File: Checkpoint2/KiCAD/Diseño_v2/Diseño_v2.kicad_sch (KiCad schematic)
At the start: 0 parts

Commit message: PCB LDO (final?)
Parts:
- added Gen_In1, TP_GND1, TP_Out_PD1, TP_Vo1, TP_Vx1: (no value), Connector_PinHeader_2.54mm:PinHeader_1x01_P2.54mm_Vertical, symbol Connector:TestPoint
- added J1, J2: Conn_01x02, TerminalBlock:TerminalBlock_MaiXu_MX126-5.0-02P_1x02_P5.00mm, symbol Connector_Generic:Conn_01x02
- added J3: Conn_01x03, Connector_PinHeader_2.54mm:PinHeader_1x03_P2.54mm_Vertical, symbol Connector_Generic:Conn_01x03
- added J_FC1, J_LC1, J_LT1: (no value), TestPoint:TestPoint_2Pads_Pitch2.54mm_Drill0.8mm, symbol Jumper:Jumper_2_Bridged
- added Q1, Q2, Q5, Q7, Q8, Q9: BC547, Package_TO_SOT_THT:TO-92_Inline, symbol Transistor_BJT:BC547
- added Q3, Q4: BC557, Package_TO_SOT_THT:TO-92_Inline, symbol Transistor_BJT:BC557
- added Q6: TIP32A, Package_TO_SOT_THT:TO-220-3_Vertical, symbol Transistor_BJT:Q_PNP_BCE
- added R1, RE1, RE2, RE3, RE4: 680, Resistor_THT:R_Axial_DIN0207_L6.3mm_D2.5mm_P7.62mm_Horizontal, symbol Device:R
- added R2: 4k7, Resistor_THT:R_Axial_DIN0207_L6.3mm_D2.5mm_P7.62mm_Horizontal, symbol Device:R
- added R3, R4, Rx1: 10k, Resistor_THT:R_Axial_DIN0207_L6.3mm_D2.5mm_P7.62mm_Horizontal, symbol Device:R
- added RS1: 1.8, Resistor_THT:R_Axial_DIN0414_L11.9mm_D4.5mm_P15.24mm_Horizontal, symbol Device:R
- added RS2: 2.2, Resistor_THT:R_Axial_DIN0414_L11.9mm_D4.5mm_P15.24mm_Horizontal, symbol Device:R
- added Rf1: 10k, Resistor_THT:R_Axial_DIN0207_L6.3mm_D2.5mm_P2.54mm_Vertical, symbol Device:R
- added Ro1: 150, Resistor_THT:R_Axial_DIN0207_L6.3mm_D2.5mm_P7.62mm_Horizontal, symbol Device:R
- added Rref1: 1k2, Resistor_THT:R_Axial_DIN0207_L6.3mm_D2.5mm_P7.62mm_Horizontal, symbol Device:R
- added Rx2: 3k9, Resistor_THT:R_Axial_DIN0207_L6.3mm_D2.5mm_P7.62mm_Horizontal, symbol Device:R
- added TP_Vref1: (no value), symbol Connector:TestPoint
- added U1: TL431LP, Package_TO_SOT_THT:TO-92_Inline, symbol Reference_Voltage:TL431LP
- added U2: LM358, Package_DIP:DIP-8_W7.62mm_LongPads, symbol Amplifier_Operational:LM358
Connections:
- new net: Rf1.1, Ro1.2, Rref1.2, U2.2 (-)
- new net: Rx1.2, Rx2.2, U2.3 (+)
- new net: J1.2 (Pin_2), Q6.3 (E), R1.1, R2.1, RE1.1, RE2.1, U2.8 (V+)
- new net: J_LT1.1 (A), Q2.2 (B)
- new net: J_LT1.2 (B), R3.1, R4.1
- new net: Q2.1 (C), Q4.1 (C), Q5.2 (B), Q9.1 (C), TP_Out_PD1.1
- new net: J_LC1.1 (A), Q9.2 (B)
- new net: Q1.1 (C), Q3.1 (C), Q3.2 (B), Q4.2 (B)
- new net: Q3.3 (E), RE1.2
- new net: Q7.3 (E), RE4.1
- new net: Q8.3 (E), RE3.1
- new net: Gen_In1.1, J3.1 (Pin_1)
- new net: J_FC1.2 (B), Q7.1 (C)
- new net: Q7.2 (B), Q8.1 (C), Q8.2 (B), R2.2
- new net: J_FC1.1 (A), Q1.3 (E), Q2.3 (E)
- new net: Q5.1 (C), Q6.1 (B)
- new net: Q4.3 (E), RE2.2
- new net: J3.3 (Pin_3), R1.2, U1.1 (REF), U1.3 (K)
- new net GND: J1.1 (Pin_1), J2.1 (Pin_1), Q9.3 (E), R4.2, RE3.2, RE4.2, Rx2.1, TP_GND1.1, U1.2 (A), U2.4 (V-)
- new net Vf: J_LC1.2 (B), Rf1.2, U2.1
- new net Vo: J2.2 (Pin_2), R3.2, RS1.2, RS2.2, Ro1.1, TP_Vo1.1
- new net Vref: J3.2 (Pin_2), Q1.2 (B), Rref1.1, TP_Vref1.1
- new net Vx: Q5.3 (E), Q6.2 (C), RS1.1, RS2.1, Rx1.1, TP_Vx1.1
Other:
- note added: "Nota sobre las aberviaciones: LC: Lazo de corriente LT: Lazo de tensión PD: par diferencial FC: fuente de corriente"
- company: (none) -> FIUBA - TA138
- title: (none) -> Fuente regulada con protección Foldback - Grupo 5

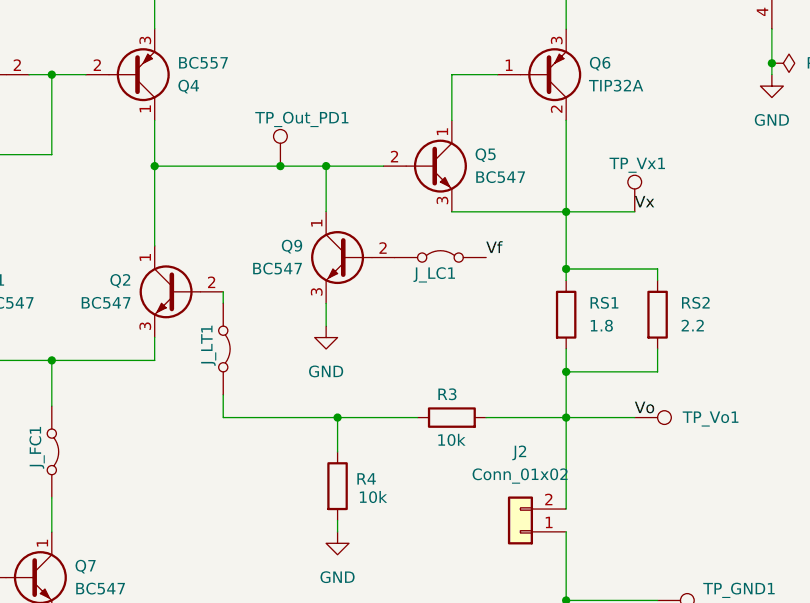
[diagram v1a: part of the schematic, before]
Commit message: agregué el capacitor de compensación
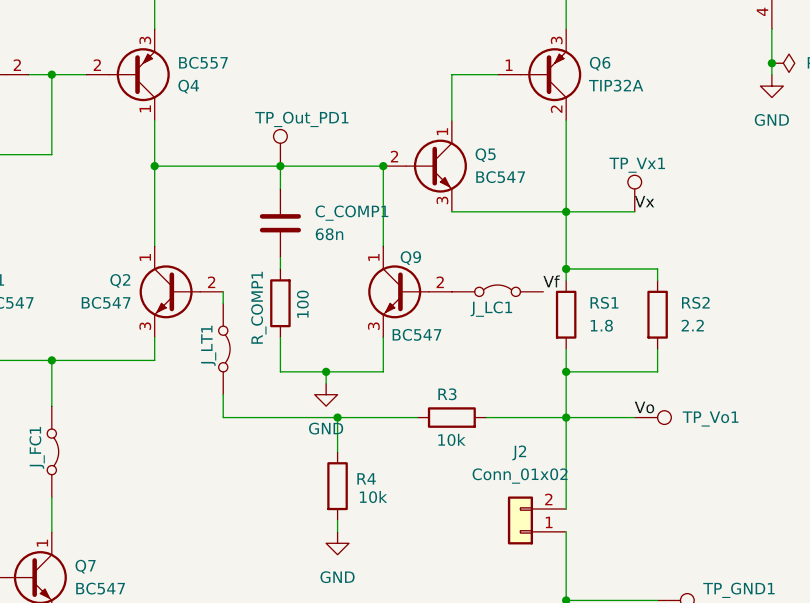
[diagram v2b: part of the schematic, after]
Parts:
- added C_COMP1: 68n, Capacitor_THT:C_Disc_D5.0mm_W2.5mm_P2.50mm, symbol Device:C
- added R_COMP1: 100, Resistor_THT:R_Axial_DIN0207_L6.3mm_D2.5mm_P7.62mm_Horizontal, symbol Device:R
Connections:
- net GND: now also R_COMP1.1
- net at Q2.1 (C), Q4.1 (C), Q5.2 (B)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: now also C_COMP1.2
- new net: C_COMP1.1, R_COMP1.2
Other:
- moved on the sheet: J_LC1, Q9

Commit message: Cambié las huellas de los TBJ xq estaban muy juntas
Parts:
- Q1, Q2, Q3, Q4, Q5, Q7, Q8, Q9, U1: footprint Package_TO_SOT_THT:TO-92_Inline -> Package_TO_SOT_THT:TO-92_Inline_Wide
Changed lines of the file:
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@@
 			)
 		)
-		(property "Footprint" "Package_TO_SOT_THT:TO-92_Inline"
+		(property "Footprint" "Package_TO_SOT_THT:TO-92_Inline_Wide"
 			(at 154.94 102.235 0)
 			(hide yes)
@@
 			)
 		)
-		(property "Footprint" "Package_TO_SOT_THT:TO-92_Inline"
+		(property "Footprint" "Package_TO_SOT_THT:TO-92_Inline_Wide"
 			(at 107.95 74.295 0)
 			(hide yes)
@@
 			)
 		)
-		(property "Footprint" "Package_TO_SOT_THT:TO-92_Inline"
+		(property "Footprint" "Package_TO_SOT_THT:TO-92_Inline_Wide"
 			(at 123.19 133.985 0)
 			(hide yes)
@@
 			)
 		)
-		(property "Footprint" "Package_TO_SOT_THT:TO-92_Inline"
+		(property "Footprint" "Package_TO_SOT_THT:TO-92_Inline_Wide"
 			(at 113.03 102.235 0)
 			(hide yes)
@@
 			)
 		)
-		(property "Footprint" "Package_TO_SOT_THT:TO-92_Inline"
+		(property "Footprint" "Package_TO_SOT_THT:TO-92_Inline_Wide"
 			(at 167.64 88.265 0)
 			(hide yes)
@@
 			)
 		)
-		(property "Footprint" "Package_TO_SOT_THT:TO-92_Inline"
+		(property "Footprint" "Package_TO_SOT_THT:TO-92_Inline_Wide"
 			(at 134.62 74.295 0)
 			(hide yes)
@@
 			)
 		)
-		(property "Footprint" "Package_TO_SOT_THT:TO-92_Inline"
+		(property "Footprint" "Package_TO_SOT_THT:TO-92_Inline_Wide"
 			(at 78.74 133.985 0)
 			(hide yes)
@@
 			)
 		)
-		(property "Footprint" "Package_TO_SOT_THT:TO-92_Inline"
+		(property "Footprint" "Package_TO_SOT_THT:TO-92_Inline_Wide"
 			(at 129.54 102.235 0)
 			(hide yes)
@@
 			)
 		)
-		(property "Footprint" "Package_TO_SOT_THT:TO-92_Inline"
+		(property "Footprint" "Package_TO_SOT_THT:TO-92_Inline_Wide"
 			(at 93.726 104.14 0)
 			(hide yes)
